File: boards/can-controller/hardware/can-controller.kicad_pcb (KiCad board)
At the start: 2 copper layers, 100 x 100 mm, 188 parts, among them J1 RPi_GPIO, J10 CAN1, J11 CAN2, J12 CAN3, J13 CAN4, J2 ICSP, J20 12V IN, J3 UART, J30 RELAY, J4 USB-C, J40 GPIO 1-4, J41 GPIO 5-8, J50 ANALOG, Q1 SUD50P04-08, U1 PIC32MK1024MCM064-I/PT, U10 ISO1044BD, U11 ISO1044BD, U12 ISO1044BD, U13 ISO1044BD, U2 MCP1826S-3302E/DB, U20 R-78E5.0-0.5, U21 TLP293, U3 USBLC6-2SC6, U30 ISO6740, U31 ISO6740, U32 ULN2803A, U50 MCP3428-E/SL, U60 MCP4922-E/SL, U61 LM4040-2.5, U62 LM358B, U63 TPS61040, Y1 12MHz

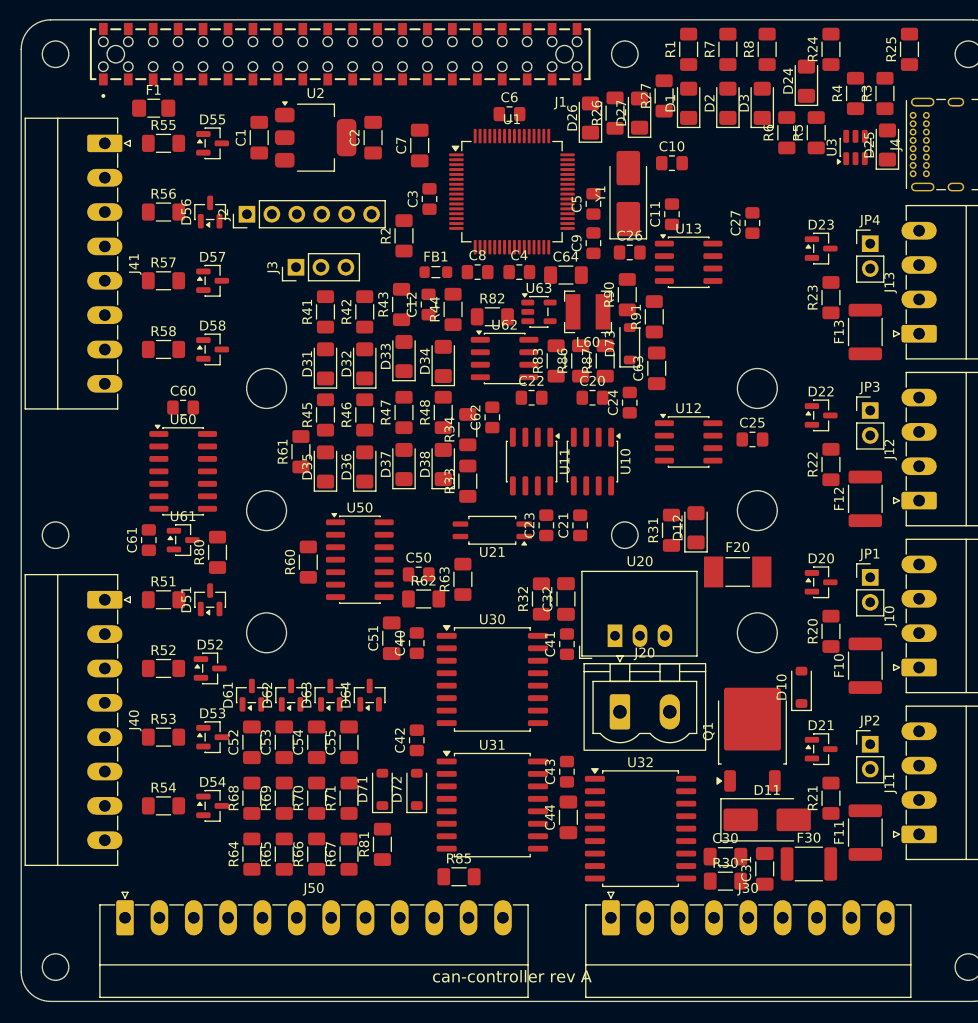
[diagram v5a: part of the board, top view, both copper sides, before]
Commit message: can-controller: double-level push-in terminals, re-placement, no DIN clips
- Phoenix SPTD 1,5 footprints (3-8 positions) generated from the Phoenix
  drawing (lib/footprint_src/Thl_Connector/phoenix_sptd.py)
- Schematic: J40 GPIO 2x8 (GPIO1-8 / GND), J50 ANALOG 2x6 (AI1-4, AO1-2 /
  GND), J30 RELAY 2x8 (OUT1-8 / +12 V); relay LEDs moved to the 12 V side
  (+12 V -> 4.7k -> LED -> OUTn); J41 removed
- Placement rev 2: GPIO and analog on the left edge, relay on the bottom;
  12 V block x > 140, y > 160 plus the CAN strip; all ISO1044 on x = 168;
  relay LEDs behind their terminal pins; CAN LEDs in a column
- DIN clip holes removed (3D-printed adapter on the M2.5 holes instead)
- DRC clean apart from unrouted nets and silkscreen

Co-Authored-By: Claude Opus 5.5 <noreply@anthropic.com>
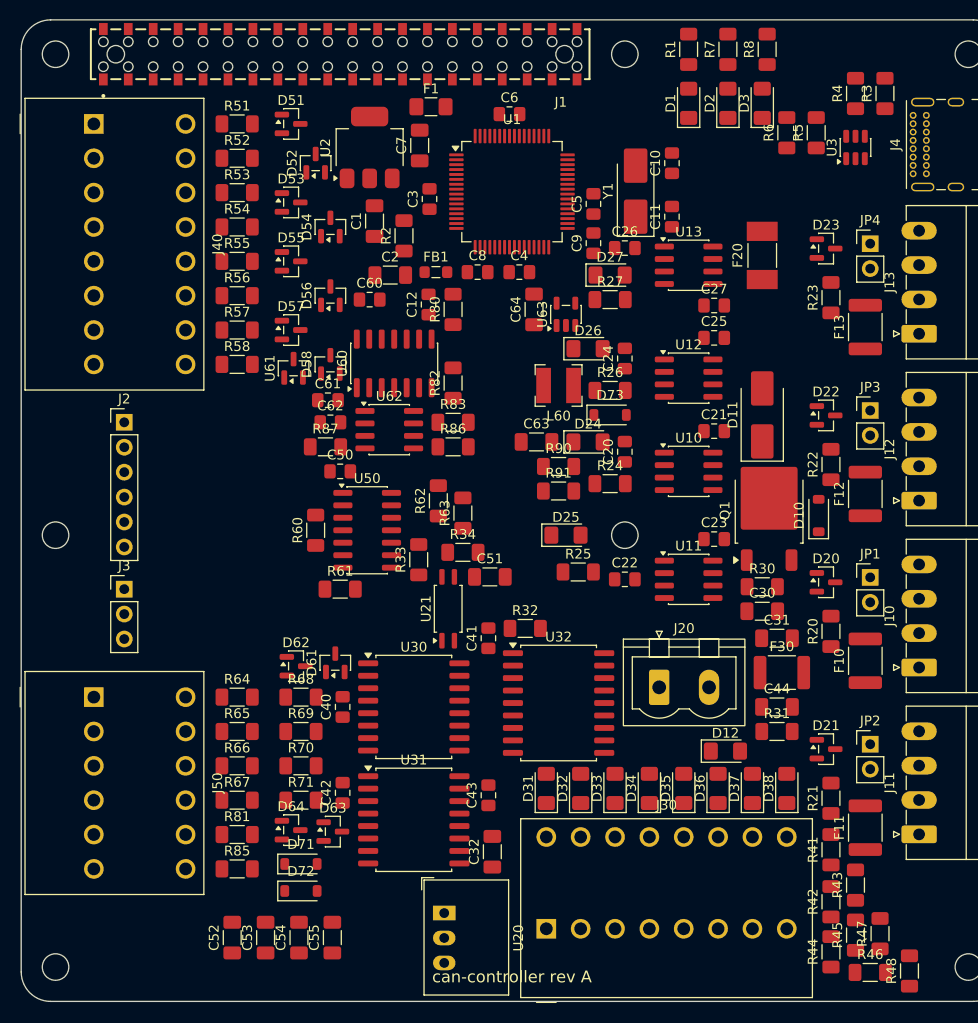
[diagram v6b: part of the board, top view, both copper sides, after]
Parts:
- removed J41: GPIO 5-8, Connector_Phoenix_MC:PhoenixContact_MC_1,5_8-G-3.5_1x08_P3.50mm_Horizontal
- removed MK1, MK2: DIN rail clip, Thl_Mechanical:DIN_Rail_Mount_3xNPTH4.06mm_P12.45mm
- J30: footprint Connector_Phoenix_MC:PhoenixContact_MC_1,5_9-G-3.5_1x09_P3.50mm_Horizontal -> Thl_Connector:PhoenixContact_SPTD_1,5_8-H-3,5_2x08_P3.5mm_Horizontal
- J40: value GPIO 1-4 -> GPIO; footprint Connector_Phoenix_MC:PhoenixContact_MC_1,5_8-G-3.5_1x08_P3.50mm_Horizontal -> Thl_Connector:PhoenixContact_SPTD_1,5_8-H-3,5_2x08_P3.5mm_Horizontal
- J50: footprint Connector_Phoenix_MC:PhoenixContact_MC_1,5_12-G-3.5_1x12_P3.50mm_Horizontal -> Thl_Connector:PhoenixContact_SPTD_1,5_6-H-3,5_2x06_P3.5mm_Horizontal
- R41, R42, R43, R44, R45, R46, R47, R48: value 1k -> 4.7k
- moved R46 76.7 mm to (186.5, 197.1), turned to 0 degrees
- moved R42 76.6 mm to (182.5, 189.8)
- moved R44 75.9 mm to (182.5, 194.9)
- moved R45 75.7 mm to (185.0, 193.2)
- moved R41 75.2 mm to (182.5, 184.6)
- moved R43 75.1 mm to (185.0, 188.2)
- moved R48 74.1 mm to (190.5, 196.9)
- moved R47 71.9 mm to (187.5, 193.1)
- moved R25 63.0 mm to (156.8, 156.2), turned to 0 degrees
- moved D54 60.2 mm to (131.5, 121.1), turned to 90 degrees
- moved R54 59.5 mm to (122.0, 121.1)
- moved R53 56.0 mm to (122.0, 117.6)
- moved D53 55.1 mm to (127.5, 118.6)
- moved D52 52.6 mm to (130.0, 114.6), turned to 90 degrees
- moved R52 52.5 mm to (122.0, 114.1)
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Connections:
- D31 pad 1: GND -> /Relay drive/RLYO1
- D32 pad 1: GND -> /Relay drive/RLYO2
- D33 pad 1: GND -> /Relay drive/RLYO3
- D34 pad 1: GND -> /Relay drive/RLYO4
- D35 pad 1: GND -> /Relay drive/RLYO5
- D36 pad 1: GND -> /Relay drive/RLYO6
- D37 pad 1: GND -> /Relay drive/RLYO7
- D38 pad 1: GND -> /Relay drive/RLYO8
- J40 pad 2: GND -> /GPIO/GPIO2_EXT
- J40 pad 3: /GPIO/GPIO2_EXT -> /GPIO/GPIO3_EXT
- J40 pad 4: GND -> /GPIO/GPIO4_EXT
- J40 pad 5: /GPIO/GPIO3_EXT -> /GPIO/GPIO5_EXT
- J40 pad 6: GND -> /GPIO/GPIO6_EXT
- J40 pad 7: /GPIO/GPIO4_EXT -> /GPIO/GPIO7_EXT
- J40 pad 8: GND -> /GPIO/GPIO8_EXT
- J50 pad 11: /Analog out/AO2_EXT -> GND
- J50 pad 2: GND -> AI2_EXT
- J50 pad 3: AI2_EXT -> AI3_EXT
- J50 pad 4: GND -> AI4_EXT
- J50 pad 5: AI3_EXT -> /Analog out/AO1_EXT
- J50 pad 6: GND -> /Analog out/AO2_EXT
- J50 pad 7: AI4_EXT -> GND
- J50 pad 9: /Analog out/AO1_EXT -> GND
- R41 pad 1: RLY1 -> /Relay drive/V12_RLY
- R42 pad 1: RLY2 -> /Relay drive/V12_RLY
- R43 pad 1: RLY3 -> /Relay drive/V12_RLY
- R44 pad 1: RLY4 -> /Relay drive/V12_RLY
- R45 pad 1: RLY5 -> /Relay drive/V12_RLY
- R46 pad 1: RLY6 -> /Relay drive/V12_RLY
- R47 pad 1: RLY7 -> /Relay drive/V12_RLY
- R48 pad 1: RLY8 -> /Relay drive/V12_RLY
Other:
- board text added: "Domain boundary (placement rev 2): only U10-U13, U21, U30, U31 cross it"
- board text removed: "Domain boundary (placement rev 1): only U10-U13, U21, U30, U31 cross it"

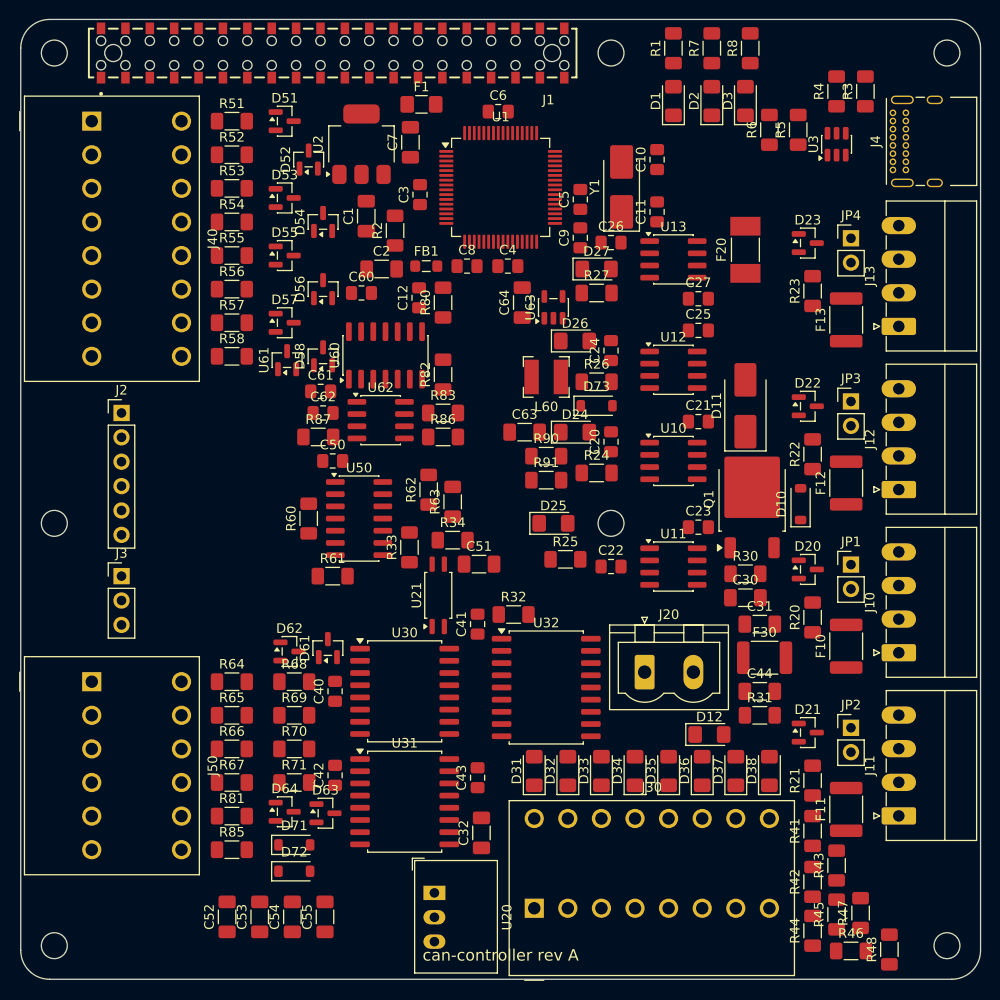
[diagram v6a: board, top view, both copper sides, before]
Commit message: can-controller: routing WIP (planes, ground fanout, top-only autoroute)
- Bottom planes: GND (logic) and GND_BUS (12 V), 2 mm gap at the domain
  boundary; no top-layer fills
- 108 ground fanout vias from top-side SMD ground pads
- Freerouting, one domain at a time with the other domain as a keep-out,
  top layer only: no bottom traces, nothing crosses the domain boundary
- Power net-class patterns for GND_BUS, V5_BUS, V12*, V13, VBUS, AVDD
- DRC: no errors. Open: 75 logic connections (mostly MCU escapes), 35 in
  the 12 V domain, 5 MCU ground pins

Co-Authored-By: Claude Opus 5.5 <noreply@anthropic.com>
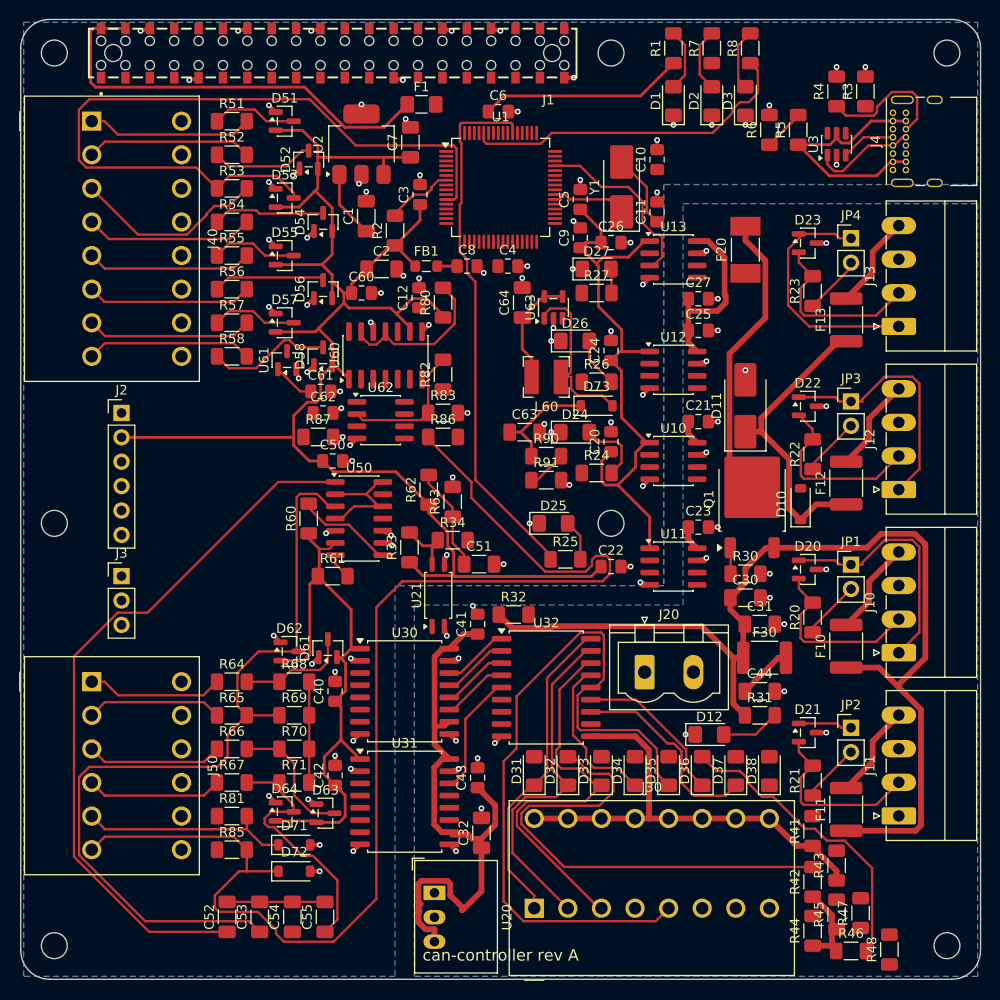
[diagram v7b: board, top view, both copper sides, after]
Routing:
- net +3V3: track 0.00 -> 308.3 mm
- net +12V: track 0.00 -> 142.5 mm
- net /Analog out/AO2_EXT: track 0.00 -> 133.5 mm
- net /Analog in/AIN2: track 0.00 -> 88.1 mm
- net /Analog in/AIN1: track 0.00 -> 86.5 mm
- net V5_BUS: track 0.00 -> 84.8 mm
- net GND: track 0.00 -> 81.0 mm, vias 0 -> 81
- net GPIO3: track 0.00 -> 78.8 mm
- net /Relay drive/RLYO5: track 0.00 -> 77.3 mm
- net /Relay drive/V12_RLY: track 0.00 -> 63.5 mm
- net LED_CAN2: track 0.00 -> 55.9 mm
- net /Relay drive/D32_A: track 0.00 -> 50.9 mm
- net /MCU, USB, power/V5_PI: track 0.00 -> 45.0 mm
- net /Analog in/VMID: track 0.00 -> 44.5 mm
- net /Relay drive/RLYO3: track 0.00 -> 41.7 mm
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- added copper zone on B.Cu, net GND
- added copper zone on B.Cu, net GND_BUS

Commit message: can-controller: placement rev 3 so the MCU can fan out, routing WIP
Schematic:
- U1 pin map redone for the MCU rotated 90 deg: each side carries the
  signals for the parts it faces, in order (GPIO left, CAN right, USB /
  crystal / ICSP / UART top, DAC SPI4 / I2C1 bottom). ICSP on PGx2
  (pins 43/44, ICESEL = PGx2), UART1 on 46/47, V12_OK on pin 33.
- Relays driven over I2C1 by an MCP23008 (U33, 0x20); relay channel
  order permuted so expander -> ISO6740 -> ULN2803A -> J30 runs straight
- FB1 removed, AVDD tied to +3V3 (sits between two CAN pin pairs)
- J50 pinout: 1-2 AO1/AO2, 3-6 AI1-4 (outputs no longer cross inputs)
- Interface_Expansion:MCP23008-xSO imported to lib/

PCB:
- place_rev3.py: U1 rotated at (148,131), expander under it, relay
  isolators across the 12 V block's top edge (corner now x = 134),
  ULN below, 12 V opto at the top of the CAN strip, analog section
  re-laid around the new J50 pinout; bottom zones follow the new corner
- Routed: MCU escape nets first, signals top only, then power; 8
  connections open, ~48 clearance near-misses to clean up by hand,
  ~370 mm bottom traces

Co-Authored-By: Claude Opus 5.5 <noreply@anthropic.com>
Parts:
- removed FB1: 600R@100MHz, Inductor_SMD:L_0805_2012Metric_Pad1.05x1.20mm_HandSolder
- added C45: 100nF 50V X7R, Capacitor_SMD:C_0805_2012Metric_Pad1.18x1.45mm_HandSolder, F.Cu at (153.5, 140.0)
- added U33: MCP23008-E/SO, Package_SO:SOIC-18W_7.5x11.6mm_P1.27mm, F.Cu at (146.1, 144.6)
- moved D3 65.1 mm to (122.0, 145.6), turned to 0 degrees
- moved R8 64.6 mm to (127.4, 145.6), turned to 180 degrees
- moved R63 57.6 mm to (112.0, 197.5), turned to 0 degrees
- moved U21 51.8 mm to (170.5, 115.8)
- moved R32 51.0 mm to (180.0, 119.8)
- moved C51 50.5 mm to (118.0, 197.5)
- moved L60 49.9 mm to (109.6, 158.6)
- moved J3 49.1 mm to (132.4, 114.0), turned to -90 degrees
- moved U63 49.1 mm to (112.5, 153.8), turned to 0 degrees
- moved J2 48.6 mm to (147.6, 109.6), turned to -90 degrees
- moved R33 47.3 mm to (166.5, 115.5)
- moved D73 47.3 mm to (116.0, 157.5)
- moved R91 47.2 mm to (110.0, 163.0)
- moved R1 46.7 mm to (122.5, 113.4), turned to 0 degrees
- moved C64 44.4 mm to (112.5, 149.3)
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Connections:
- C8 pad 1: /MCU, USB, power/AVDD -> +3V3
- J2 pad 4: /MCU, USB, power/PGD1 -> /MCU, USB, power/PGD2
- J2 pad 5: /MCU, USB, power/PGC1 -> /MCU, USB, power/PGC2
- J50 pad 1: AI1_EXT -> /Analog out/AO1_EXT
- J50 pad 2: AI2_EXT -> /Analog out/AO2_EXT
- J50 pad 3: AI3_EXT -> AI1_EXT
- J50 pad 4: AI4_EXT -> AI2_EXT
- J50 pad 5: /Analog out/AO1_EXT -> AI3_EXT
- J50 pad 6: /Analog out/AO2_EXT -> AI4_EXT
- U1 pad 1: GPIO8 -> unconnected-(U1-RA7/TCK/RPA7-Pad1)
- U1 pad 11: GPIO3 -> unconnected-(U1-RA12/AN10/RPA12-Pad11)
- U1 pad 12: GPIO2 -> unconnected-(U1-RA11/AN9/RPA11-Pad12)
- U1 pad 13: GPIO1 -> LED_CAN2
- U1 pad 14: DAC_CS -> C2RX
- U1 pad 15: unconnected-(U1-RB0/PGD3/VREF-/OA2IN-/AN2/C2IN1-/RPB0/CTED2-Pad15) -> C2TX
- U1 pad 16: unconnected-(U1-RB1/PGC3/OA1OUT/VREF+/AN3/C1IN4-/C4IN2-/RPB1/CTED1-Pad16) -> LED_CAN1
- U1 pad 17: /MCU, USB, power/PGC1 -> C1RX
- U1 pad 18: /MCU, USB, power/PGD1 -> C1TX
- U1 pad 19: /MCU, USB, power/AVDD -> +3V3
- U1 pad 2: GPIO7 -> DAC_SDI
- U1 pad 22: RLY1 -> C3TX
- U1 pad 23: RLY2 -> unconnected-(U1-RC2/OA3IN+/AN8/C3IN1+/C3IN3-/RPC2-Pad23)
- U1 pad 24: RLY3 -> unconnected-(U1-RC11/AN11/C1IN2--Pad24)
- U1 pad 27: RLY4 -> unconnected-(U1-RE12/AN12/C2IN2-/C5IN2-/SDA4-Pad27)
- U1 pad 28: RLY5 -> unconnected-(U1-RE13/AN13/C3IN2-/SCL4-Pad28)
- U1 pad 29: C3TX -> LED_CAN3
- U1 pad 3: GPIO6 -> DAC_SCK
- U1 pad 30: C2TX -> C4RX
- U1 pad 31: C2RX -> C4TX
- U1 pad 32: C1TX -> LED_CAN4
- U1 pad 33: C1RX -> V12_OK
- U1 pad 4: GPIO5 -> DAC_CS
- U1 pad 42: RLY6 -> unconnected-(U1-RD8-Pad42)
- U1 pad 43: C4TX -> /MCU, USB, power/PGD2
- U1 pad 44: RLY7 -> /MCU, USB, power/PGC2
- U1 pad 45: C4RX -> /MCU, USB, power/LED_HB
- U1 pad 46: DAC_SCK -> /MCU, USB, power/U1TX
- U1 pad 47: V12_OK -> /MCU, USB, power/U1RX
- U1 pad 49: RLY8 -> GPIO1
- U1 pad 50: /MCU, USB, power/U1RX -> GPIO2
- U1 pad 51: /MCU, USB, power/U1TX -> GPIO3
- U1 pad 52: DAC_SDI -> GPIO4
- U1 pad 53: LED_CAN1 -> GPIO5
- U1 pad 54: LED_CAN2 -> GPIO6
- U1 pad 55: LED_CAN3 -> GPIO7
- U1 pad 58: LED_CAN4 -> GPIO8
- U1 pad 59: /MCU, USB, power/LED_HB -> /MCU, USB, power/LED_USB
- U1 pad 60: /MCU, USB, power/LED_USB -> unconnected-(U1-RB10/RPB10-Pad60)
- U1 pad 8: GPIO4 -> unconnected-(U1-RG9/AN16/RPG9-Pad8)
- U30 pad 11: /Relay drive/RLYD4 -> /Relay drive/RLYD1
- U30 pad 12: /Relay drive/RLYD3 -> /Relay drive/RLYD2
- U30 pad 13: /Relay drive/RLYD2 -> /Relay drive/RLYD3
- U30 pad 14: /Relay drive/RLYD1 -> /Relay drive/RLYD4
- U30 pad 3: RLY1 -> /Relay drive/RLY4
- U30 pad 4: RLY2 -> /Relay drive/RLY3
- U30 pad 5: RLY3 -> /Relay drive/RLY2
- U30 pad 6: RLY4 -> /Relay drive/RLY1
- U31 pad 11: /Relay drive/RLYD8 -> /Relay drive/RLYD5
- U31 pad 12: /Relay drive/RLYD7 -> /Relay drive/RLYD6
- U31 pad 13: /Relay drive/RLYD6 -> /Relay drive/RLYD7
- U31 pad 14: /Relay drive/RLYD5 -> /Relay drive/RLYD8
- U31 pad 3: RLY5 -> /Relay drive/RLY8
- U31 pad 4: RLY6 -> /Relay drive/RLY7
- U31 pad 5: RLY7 -> /Relay drive/RLY6
- U31 pad 6: RLY8 -> /Relay drive/RLY5
- U32 pad 1: /Relay drive/RLYD1 -> /Relay drive/RLYD8
- U32 pad 11: /Relay drive/RLYO8 -> /Relay drive/RLYO1
- U32 pad 12: /Relay drive/RLYO7 -> /Relay drive/RLYO2
- U32 pad 13: /Relay drive/RLYO6 -> /Relay drive/RLYO3
- U32 pad 14: /Relay drive/RLYO5 -> /Relay drive/RLYO4
- U32 pad 15: /Relay drive/RLYO4 -> /Relay drive/RLYO5
- U32 pad 16: /Relay drive/RLYO3 -> /Relay drive/RLYO6
- U32 pad 17: /Relay drive/RLYO2 -> /Relay drive/RLYO7
- U32 pad 18: /Relay drive/RLYO1 -> /Relay drive/RLYO8
- U32 pad 2: /Relay drive/RLYD2 -> /Relay drive/RLYD7
- U32 pad 3: /Relay drive/RLYD3 -> /Relay drive/RLYD6
- U32 pad 4: /Relay drive/RLYD4 -> /Relay drive/RLYD5
- U32 pad 5: /Relay drive/RLYD5 -> /Relay drive/RLYD4
- U32 pad 6: /Relay drive/RLYD6 -> /Relay drive/RLYD3
- U32 pad 7: /Relay drive/RLYD7 -> /Relay drive/RLYD2
- U32 pad 8: /Relay drive/RLYD8 -> /Relay drive/RLYD1
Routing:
- net +3V3: track 308.3 -> 577.7 mm, vias 0 -> 48
- net /Relay drive/D33_A: track 0.00 -> 104.3 mm
- net /Analog out/AO2_EXT: track 133.5 -> 34.3 mm
- net +12V: track 142.5 -> 230.7 mm, vias 0 -> 17
- net V5_BUS: track 84.8 -> 170.3 mm, vias 0 -> 10
- net /Relay drive/RLYO8: track 0.00 -> 81.2 mm
- net /Relay drive/V12_RLY: track 63.5 -> 142.1 mm, vias 0 -> 19
- net /Analog in/VMID: track 44.5 -> 110.2 mm, vias 0 -> 16
- net +5V: track 18.8 -> 83.7 mm, vias 0 -> 4
- net GPIO3: track 78.8 -> 20.3 mm
- net /Relay drive/RLYO7: track 21.1 -> 74.6 mm
- net /CAN x4/CANH2: track 5.62 -> 58.2 mm
- net /Relay drive/RLYO6: track 16.5 -> 67.9 mm
- net GPIO6: track 11.7 -> 56.8 mm
- net /12 V input/V12_IN: track 0.00 -> 44.9 mm, vias 0 -> 8
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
